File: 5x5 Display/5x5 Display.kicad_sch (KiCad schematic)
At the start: 44 parts, among them Q1 PMOS

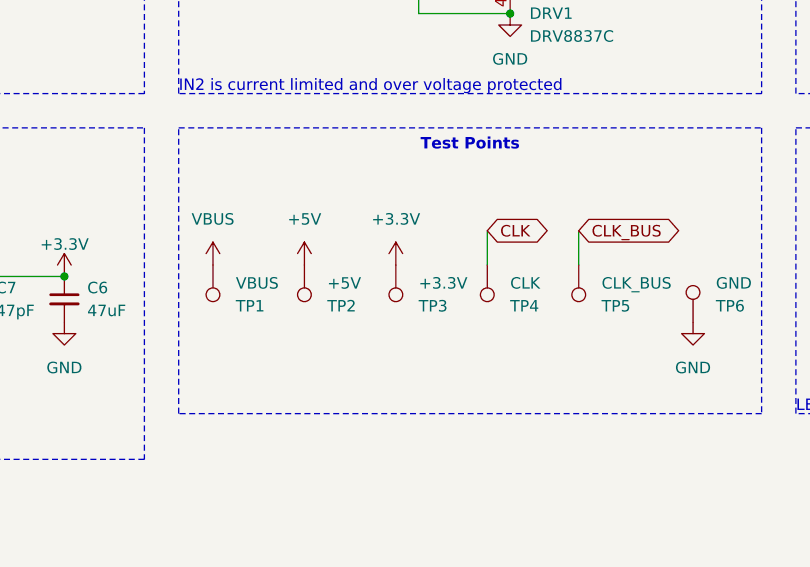
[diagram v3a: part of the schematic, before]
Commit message: Add test points
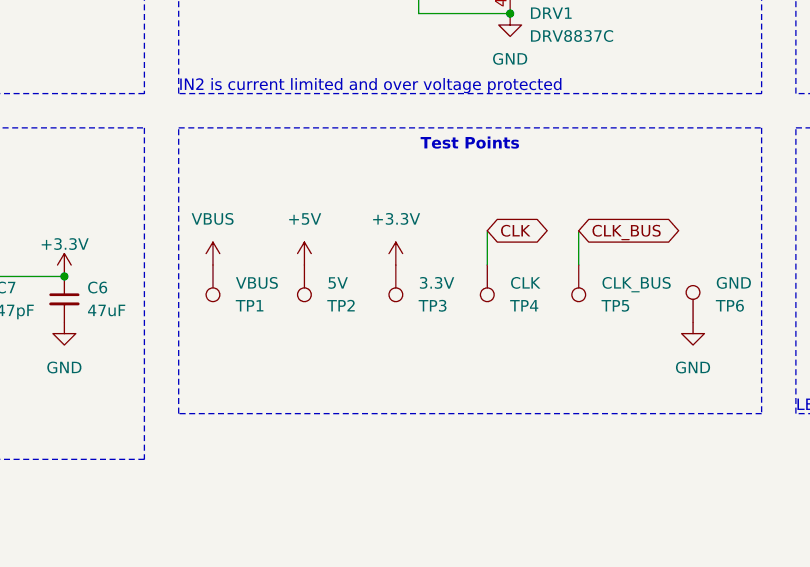
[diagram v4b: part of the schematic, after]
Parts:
- TP2: value +5V -> 5V
- TP3: value +3.3V -> 3.3V
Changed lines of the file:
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@@
 			)
 		)
-		(property "Value" "+5V"
+		(property "Value" "5V"
 			(at 187.96 78.2321 0)
 			(effects
@@
 			)
 		)
-		(property "Value" "+3.3V"
+		(property "Value" "3.3V"
 			(at 198.12 78.2321 0)
 			(effects

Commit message: update LCSC part number for bootstrap capacitors
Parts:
- C3, C4: LCSC Part # C24497 -> C28233
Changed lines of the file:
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@@
 			)
 		)
-		(property "LCSC Part #" "C24497"
+		(property "LCSC Part #" "C28233"
 			(at 127 77.47 90)
 			(effects
@@
 			)
 		)
-		(property "LCSC Part #" "C24497"
+		(property "LCSC Part #" "C28233"
 			(at 127 31.75 90)
 			(effects

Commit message: R2 Ordered
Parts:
- C7: LCSC Part # C1567 -> C1671
- D8: LCSC Part # C96123 -> C84256
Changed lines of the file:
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@@
 			)
 		)
-		(property "LCSC Part #" "C1567"
+		(property "LCSC Part #" "C1671"
 			(at 148.59 80.01 0)
 			(effects
@@
 			)
 		)
-		(property "LCSC Part #" "C96123"
+		(property "LCSC Part #" "C84256"
 			(at 270.51 81.28 90)
 			(effects
@@
 			)
 		)
+		(property "Name" ""
+			(at 270.51 81.28 0)
+			(effects
+				(font
+					(size 1.27 1.27)
+				)
+			)
+		)
